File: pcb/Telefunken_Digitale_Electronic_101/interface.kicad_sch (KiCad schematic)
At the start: 7 parts, among them J10 Conn_01x03_Socket, J6 Conn_01x02_Socket, J7 Conn_01x02_Socket, J8 Conn_01x04_Socket, J9 Conn_01x04_Socket

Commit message: PCB: initial layout idea
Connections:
- net BT_FAST: now also J9.3 (Pin_3); no longer J10.3 (Pin_3)
- net BT_ILLUM: now also J9.2 (Pin_2); no longer J9.1 (Pin_1)
- net BT_SIGNAL: now also J10.3 (Pin_3); no longer J9.3 (Pin_3)
- net BT_SLEEP_FRONT: now also J9.1 (Pin_1); no longer J9.2 (Pin_2)
- net BT_SLOW: now also J9.4 (Pin_4); no longer J10.2 (Pin_2)
- net BT_TIME: now also J10.2 (Pin_2); no longer J9.4 (Pin_4)
- net RTC_SCL: now also J8.2 (Pin_2); no longer J8.1 (Pin_1)
- net RTC_SDA: now also J8.1 (Pin_1); no longer J8.2 (Pin_2)
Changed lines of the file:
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@@
-		)
-	)
-	(label "BT_SIGNAL"
-		(at 48.26 111.76 0)
-		(effects
-			(font
-				(size 1.27 1.27)
-			)
-			(justify left bottom)
 		)
 	)
 	(label "RTC_SDA"
-		(at 48.26 91.44 0)
+		(at 48.26 93.98 0)
 		(effects
 			(font
@@
 		)
 	)
+	(label "BT_ILLUM"
+		(at 48.26 114.3 0)
+		(effects
+			(font
+				(size 1.27 1.27)
+			)
+			(justify left bottom)
+		)
+	)
+	(label "BT_SIGNAL"
+		(at 48.26 128.27 0)
+		(effects
+			(font
+				(size 1.27 1.27)
+			)
+			(justify left bottom)
+		)
+	)
 	(label "BT_SLEEP_FRONT"
 		(at 107.95 114.3 0)
@@
 		)
 	)
+	(label "BT_SLOW"
+		(at 48.26 109.22 0)
+		(effects
+			(font
+				(size 1.27 1.27)
+			)
+			(justify left bottom)
+		)
+	)
 	(label "RTC_32K"
 		(at 106.68 85.09 0)
@@
 		)
 	)
-	(label "BT_TIME"
-		(at 48.26 109.22 0)
-		(effects
-			(font
-				(size 1.27 1.27)
-			)
-			(justify left bottom)
-		)
-	)
 	(label "BT_SLEEP_FRONT"
-		(at 48.26 114.3 0)
+		(at 48.26 116.84 0)
 		(effects
 			(font
@@
 		)
 	)
-	(label "BT_FAST"
-		(at 48.26 128.27 0)
-		(effects
-			(font
-				(size 1.27 1.27)
-			)
-			(justify left bottom)
-		)
-	)
 	(label "DISPLAY_CLK"
 		(at 102.87 68.58 0)
@@
 		)
 	)
+	(label "BT_TIME"
+		(at 48.26 130.81 0)
+		(effects
+			(font
+				(size 1.27 1.27)
+			)
+			(justify left bottom)
+		)
+	)
 	(label "RTC_SCL"
 		(at 106.68 92.71 0)
@@
 	)
 	(label "RTC_SCL"
-		(at 48.26 93.98 0)
+		(at 48.26 91.44 0)
 		(effects
 			(font
@@
 		)
 	)
+	(label "BT_FAST"
+		(at 48.26 111.76 0)
+		(effects
+			(font
+				(size 1.27 1.27)
+			)
+			(justify left bottom)
+		)
+	)
 	(label "BT_SLEEP_TOP"
 		(at 48.26 133.35 0)
@@
 		(effects
 			(font
-				(size 1.27 1.27)
-			)
-			(justify left bottom)
-		)
-	)
-	(label "BT_SLOW"
-		(at 48.26 130.81 0)
-		(effects
-			(font
-				(size 1.27 1.27)
-			)
-			(justify left bottom)
-		)
-	)
-	(label "BT_ILLUM"
-		(at 48.26 116.84 0)
-		(effects
-			(font

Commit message: SCH - buttons, display and interface: TM1637 can read the buttons (saves many resistors, caps and connectors)
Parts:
- removed J10: Conn_01x03_Socket, Connector_JST:JST_GH_BM03B-GHS-TBT_1x03-1MP_P1.25mm_Vertical, symbol Connector:Conn_01x03_Socket
- removed J9: Conn_01x04_Socket, Connector_JST:JST_GH_BM04B-GHS-TBT_1x04-1MP_P1.25mm_Vertical, symbol Connector:Conn_01x04_Socket

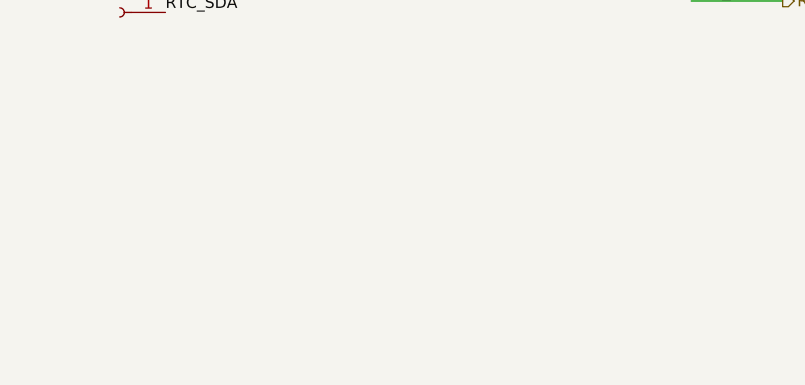
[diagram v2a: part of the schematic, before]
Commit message: SCH and PCB: added the Mounting Pads (a few chosen ones)
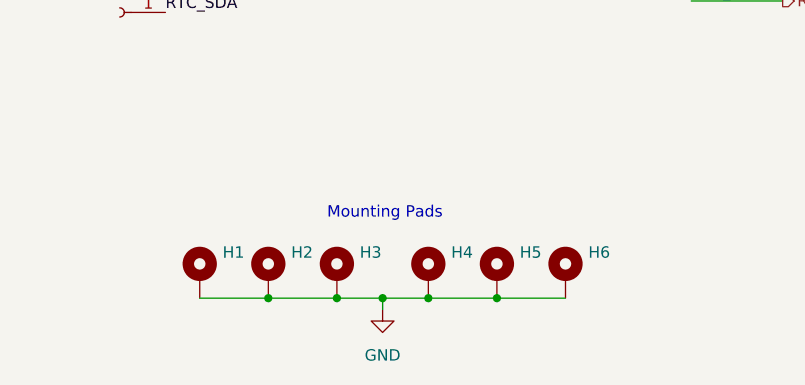
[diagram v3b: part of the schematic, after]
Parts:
- added H1, H2, H3, H4, H5, H6: MountingHole_Pad_MP, RadioWecker:BOARD_TO_BOARD_PAD_SMD, symbol Mechanical:MountingHole_Pad_MP
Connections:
- net GND: now also H1.MP, H2.MP, H3.MP, H4.MP, H5.MP, H6.MP
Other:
- note added: "Mounting Pads"

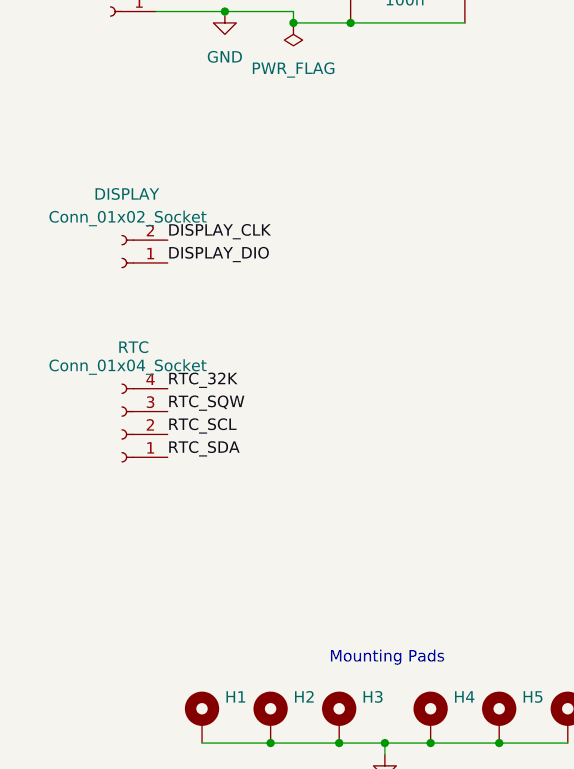
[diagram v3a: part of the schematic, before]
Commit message: SCH - interface: replaced symbols from connectors with mounting pads to contain the mounting pads (and connected them to GND)
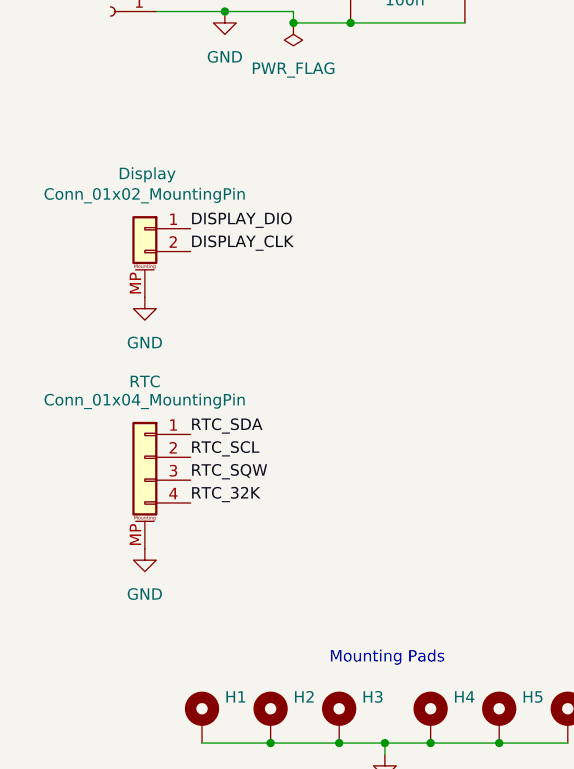
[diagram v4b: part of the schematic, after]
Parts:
- removed J7: Conn_01x02_Socket, Connector_JST:JST_GH_BM02B-GHS-TBT_1x02-1MP_P1.25mm_Vertical, symbol Connector:Conn_01x02_Socket
- removed J8: Conn_01x04_Socket, Connector_JST:JST_GH_BM04B-GHS-TBT_1x04-1MP_P1.25mm_Vertical, symbol Connector:Conn_01x04_Socket
- added J7: Conn_01x02_MountingPin, Connector_JST:JST_GH_BM02B-GHS-TBT_1x02-1MP_P1.25mm_Vertical, symbol Connector_Generic_MountingPin:Conn_01x02_MountingPin
- added J8: Conn_01x04_MountingPin, Connector_JST:JST_GH_BM04B-GHS-TBT_1x04-1MP_P1.25mm_Vertical, symbol Connector_Generic_MountingPin:Conn_01x04_MountingPin
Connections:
- net DISPLAY_CLK: now also J7.2 (Pin_2)
- net DISPLAY_DIO: now also J7.1 (Pin_1)
- net GND: now also J7.MP (MountPin), J8.MP (MountPin)
- net RTC_32K: now also J8.4 (Pin_4)
- net RTC_SCL: now also J8.2 (Pin_2)
- net RTC_SDA: now also J8.1 (Pin_1)
- net RTC_SQW: now also J8.3 (Pin_3)

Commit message: SCH and PCB: reannotated everything
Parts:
- renumbered C11 to C1, C12 to C2, J6 to J1, J7 to J2, J8 to J3
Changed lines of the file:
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@@
 		(in_pos_files yes)
 		(dnp no)
-		(property "Reference" "J8"
+		(property "Reference" "J3"
 			(at 45.72 85.09 0)
 			(hide yes)
@@
 			(project "Telefunken_Digitale_Electronic_101"
 				(path "/df1af5ff-c8b9-4769-9610-ead9e11e7e65/75a1a5d9-cb48-4e12-a237-e00fbc51bad9"
-					(reference "J8")
+					(reference "J3")
 					(unit 1)
 				)
@@
 		(dnp no)
 		(fields_autoplaced yes)
-		(property "Reference" "#PWR020"
+		(property "Reference" "#PWR03"
 			(at 54.61 45.72 0)
 			(hide yes)
@@
 			(project "Telefunken_Digitale_Electronic_101"
 				(path "/df1af5ff-c8b9-4769-9610-ead9e11e7e65/75a1a5d9-cb48-4e12-a237-e00fbc51bad9"
-					(reference "#PWR020")
+					(reference "#PWR03")
 					(unit 1)
 				)
@@
 		(dnp no)
 		(fields_autoplaced yes)
-		(property "Reference" "#PWR021"
+		(property "Reference" "#PWR04"
 			(at 54.61 50.8 0)
 			(hide yes)
@@
 			(project "Telefunken_Digitale_Electronic_101"
 				(path "/df1af5ff-c8b9-4769-9610-ead9e11e7e65/75a1a5d9-cb48-4e12-a237-e00fbc51bad9"
-					(reference "#PWR021")
+					(reference "#PWR04")
 					(unit 1)
 				)
@@
 		(in_pos_files yes)
 		(dnp no)
-		(property "Reference" "J7"
+		(property "Reference" "J2"
 			(at 45.72 62.23 0)
 			(hide yes)
@@
 			(project "Telefunken_Digitale_Electronic_101"
 				(path "/df1af5ff-c8b9-4769-9610-ead9e11e7e65/75a1a5d9-cb48-4e12-a237-e00fbc51bad9"
-					(reference "J7")
+					(reference "J2")
 					(unit 1)
 				)
@@
 		(dnp no)
 		(fields_autoplaced yes)
-		(property "Reference" "#PWR030"
+		(property "Reference" "#PWR02"
 			(at 45.72 110.49 0)
 			(hide yes)
@@
 			(project "Telefunken_Digitale_Electronic_101"
 				(path "/df1af5ff-c8b9-4769-9610-ead9e11e7e65/75a1a5d9-cb48-4e12-a237-e00fbc51bad9"
-					(reference "#PWR030")
+					(reference "#PWR02")
 					(unit 1)
 				)
@@
 		(dnp no)
 		(fields_autoplaced yes)
-		(property "Reference" "C11"
+		(property "Reference" "C1"
 			(at 72.39 40.6399 0)
 			(show_name no)
@@
 			(project "Telefunken_Digitale_Electronic_101"
 				(path "/df1af5ff-c8b9-4769-9610-ead9e11e7e65/75a1a5d9-cb48-4e12-a237-e00fbc51bad9"
-					(reference "C11")
+					(reference "C1")
 					(unit 1)
 				)
@@
 		(dnp no)
 		(fields_autoplaced yes)
-		(property "Reference" "#PWR025"
+		(property "Reference" "#PWR06"
 			(at 113.03 52.07 0)
 			(hide yes)
@@
 			(project "Telefunken_Digitale_Electronic_101"
 				(path "/df1af5ff-c8b9-4769-9610-ead9e11e7e65/75a1a5d9-cb48-4e12-a237-e00fbc51bad9"
-					(reference "#PWR025")
+					(reference "#PWR06")
 					(unit 1)
 				)
@@
 		(dnp no)
 		(fields_autoplaced yes)
-		(property "Reference" "#PWR022"
+		(property "Reference" "#PWR05"
 			(at 72.39 133.35 0)
 			(hide yes)
@@
 			(project "Telefunken_Digitale_Electronic_101"
 				(path "/df1af5ff-c8b9-4769-9610-ead9e11e7e65/75a1a5d9-cb48-4e12-a237-e00fbc51bad9"
-					(reference "#PWR022")
+					(reference "#PWR05")
 					(unit 1)
 				)
@@
 		(dnp no)
 		(fields_autoplaced yes)
-		(property "Reference" "C12"
+		(property "Reference" "C2"
 			(at 85.09 39.7509 0)
 			(show_name no)
@@
 			(project "Telefunken_Digitale_Electronic_101"
 				(path "/df1af5ff-c8b9-4769-9610-ead9e11e7e65/75a1a5d9-cb48-4e12-a237-e00fbc51bad9"
-					(reference "C12")
+					(reference "C2")
 					(unit 1)
 				)
@@
 		(dnp no)
 		(fields_autoplaced yes)
-		(property "Reference" "#PWR029"
+		(property "Reference" "#PWR01"
 			(at 45.72 82.55 0)
 			(hide yes)
@@
 			(project "Telefunken_Digitale_Electronic_101"
 				(path "/df1af5ff-c8b9-4769-9610-ead9e11e7e65/75a1a5d9-cb48-4e12-a237-e00fbc51bad9"
-					(reference "#PWR029")
+					(reference "#PWR01")
 					(unit 1)
 				)
@@
 		(in_pos_files yes)
 		(dnp no)
-		(property "Reference" "J6"
+		(property "Reference" "J1"
 			(at 42.545 36.83 0)
 			(hide yes)
@@
 			(project "Telefunken_Digitale_Electronic_101"
 				(path "/df1af5ff-c8b9-4769-9610-ead9e11e7e65/75a1a5d9-cb48-4e12-a237-e00fbc51bad9"
-					(reference "J6")
+					(reference "J1")
 					(unit 1)
 				)
@@
 		(dnp no)
 		(fields_autoplaced yes)
-		(property "Reference" "#PWR026"
+		(property "Reference" "#PWR07"
 			(at 113.03 58.42 0)
 			(hide yes)
@@
 			(project "Telefunken_Digitale_Electronic_101"
 				(path "/df1af5ff-c8b9-4769-9610-ead9e11e7e65/75a1a5d9-cb48-4e12-a237-e00fbc51bad9"
-					(reference "#PWR026")
-					(unit 1)
-				)
+					(reference "#PWR07")
+					(unit 1)
+				)

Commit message: adjusted connectors footprints, added footprint to input polarized capacitor, rtc and display polarized capacitors converted to non polarized
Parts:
- removed J1: Conn_01x02_Socket, Connector_JST:JST_XH_B2B-XH-A_1x02_P2.50mm_Vertical, symbol Connector:Conn_01x02_Socket
- added J1: Conn_01x02_MountingPin, RadioWecker:JST_S2B-XH-SM4-TB, symbol Connector_Generic_MountingPin:Conn_01x02_MountingPin
- C2: footprint (none) -> Capacitor_THT:CP_Radial_D4.0mm_P2.00mm
- J2: footprint Connector_JST:JST_GH_BM02B-GHS-TBT_1x02-1MP_P1.25mm_Vertical -> Connector_Molex:Molex_PicoBlade_53261-0271_1x02-1MP_P1.25mm_Horizontal
- J3: footprint Connector_JST:JST_GH_BM04B-GHS-TBT_1x04-1MP_P1.25mm_Vertical -> Connector_Molex:Molex_PicoBlade_53261-0471_1x04-1MP_P1.25mm_Horizontal
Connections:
- net GND: now also J1.2 (Pin_2), J1.MP (MountPin)
- net VCC: now also J1.1 (Pin_1)
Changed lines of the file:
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@@
 			)
 		)
-		(property "Footprint" "Connector_JST:JST_GH_BM04B-GHS-TBT_1x04-1MP_P1.25mm_Vertical"
+		(property "Footprint" "Connector_Molex:Molex_PicoBlade_53261-0471_1x04-1MP_P1.25mm_Horizontal"
 			(at 45.72 93.98 0)
 			(hide yes)
@@
 			)
 		)
-		(property "Footprint" "Connector_JST:JST_GH_BM02B-GHS-TBT_1x02-1MP_P1.25mm_Vertical"
+		(property "Footprint" "Connector_Molex:Molex_PicoBlade_53261-0271_1x02-1MP_P1.25mm_Horizontal"
 			(at 45.72 68.58 0)
 			(hide yes)
@@
 	)
 	(symbol
+		(lib_id "Connector_Generic_MountingPin:Conn_01x02_MountingPin")
+		(at 41.91 41.91 0)
+		(mirror y)
+		(unit 1)
+		(body_style 1)
+		(exclude_from_sim no)
+		(in_bom yes)
+		(on_board yes)
+		(in_pos_files yes)
+		(dnp no)
+		(property "Reference" "J1"
+			(at 41.91 35.56 0)
+			(hide yes)
+			(show_name no)
+			(do_not_autoplace no)
+			(effects
+				(font
+					(size 1.27 1.27)
+				)
+			)
+		)
+		(property "Value" "Conn_01x02_MountingPin"
+			(at 41.91 38.1 0)
+			(show_name no)
+			(do_not_autoplace no)
+			(effects
+				(font
+					(size 1.27 1.27)
+				)
+			)
+		)
+		(property "Footprint" "RadioWecker:JST_S2B-XH-SM4-TB"
+			(at 41.91 41.91 0)
+			(hide yes)
+			(show_name no)
+			(do_not_autoplace no)
+			(effects
+				(font
+					(size 1.27 1.27)
+				)
+			)
+		)
+		(property "Datasheet" ""
+			(at 41.91 41.91 0)
+			(hide yes)
+			(show_name no)
+			(do_not_autoplace no)
+			(effects
+				(font
+					(size 1.27 1.27)
+				)
+			)
+		)
+		(property "Description" "Generic connectable mounting pin connector, single row, 01x02, script generated (kicad-library-utils/schlib/autogen/connector/)"
+			(at 41.91 41.91 0)
+			(hide yes)
+			(show_name no)
+			(do_not_autoplace no)
+			(effects
+				(font
+					(size 1.27 1.27)
+				)
+			)
+		)
+		(property "Name" "POWER"
+			(at 42.164 35.814 0)
+			(show_name no)
+			(do_not_autoplace no)
+			(effects
+				(font
+					(size 1.27 1.27)
+				)
+			)
+		)
+		(pin "1"
+		)
+		(pin "2"
+		)
+		(pin "MP"
+		)
+		(instances
+			(project "Telefunken_Digitale_Electronic_101"
+				(path "/df1af5ff-c8b9-4769-9610-ead9e11e7e65/75a1a5d9-cb48-4e12-a237-e00fbc51bad9"
+					(reference "J1")
+					(unit 1)
+				)
+			)
+		)
+	)
+	(symbol
 		(lib_id "Mechanical:MountingHole_Pad_MP")
 		(at 77.47 123.19 0)
@@
 	(symbol
 		(lib_id "power:GND")
+		(at 41.91 49.53 0)
+		(unit 1)
+		(body_style 1)
+		(exclude_from_sim no)
+		(in_bom yes)
+		(on_board yes)
+		(in_pos_files yes)
+		(dnp no)
+		(fields_autoplaced yes)
+		(property "Reference" "#PWR023"
+			(at 41.91 55.88 0)
+			(hide yes)
+			(show_name no)
+			(do_not_autoplace no)
+			(effects
+				(font
+					(size 1.27 1.27)
+				)
+			)
+		)
+		(property "Value" "GND"
+			(at 41.91 54.61 0)
+			(show_name no)
+			(do_not_autoplace no)
+			(effects
+				(font
+					(size 1.27 1.27)
+				)
+			)
+		)
+		(property "Footprint" ""
+			(at 41.91 49.53 0)
+			(hide yes)
+			(show_name no)
+			(do_not_autoplace no)
+			(effects
+				(font
+					(size 1.27 1.27)
+				)
+			)
+		)
+		(property "Datasheet" ""
+			(at 41.91 49.53 0)
+			(hide yes)
+			(show_name no)
+			(do_not_autoplace no)
+			(effects
+				(font
+					(size 1.27 1.27)
+				)
+			)
+		)
+		(property "Description" "Power symbol creates a global label with name \"GND\" , ground"
+			(at 41.91 49.53 0)
+			(hide yes)
+			(show_name no)
+			(do_not_autoplace no)
+			(effects
+				(font
+					(size 1.27 1.27)
+				)
+			)
+		)
+		(pin "1"
+		)
+		(instances
+			(project "Telefunken_Digitale_Electronic_101"
+				(path "/df1af5ff-c8b9-4769-9610-ead9e11e7e65/75a1a5d9-cb48-4e12-a237-e00fbc51bad9"
+					(reference "#PWR023")
+					(unit 1)
+				)
+			)
+		)
+	)
+	(symbol
+		(lib_id "power:GND")
 		(at 45.72 104.14 0)
 		(unit 1)
@@
 			)
 		)
-		(property "Footprint" ""
+		(property "Footprint" "Capacitor_THT:CP_Radial_D4.0mm_P2.00mm"
 			(at 82.2452 45.72 0)
 			(hide yes)
@@
 					(unit 1)
 				)
-			)
-		)
-	)
-	(symbol
-		(lib_id "Connector:Conn_01x02_Socket")
-		(at 41.91 44.45 180)
-		(unit 1)
-		(body_style 1)
-		(exclude_from_sim no)
-		(in_bom yes)
-		(on_board yes)
-		(in_pos_files yes)
-		(dnp no)
-		(property "Reference" "J1"
-			(at 42.545 36.83 0)
-			(hide yes)
-			(show_name no)
-			(do_not_autoplace no)
-			(effects
-				(font
-					(size 1.27 1.27)
-				)
-			)
-		)
-		(property "Value" "Conn_01x02_Socket"
-			(at 42.545 39.37 0)
-			(show_name no)
-			(do_not_autoplace no)
-			(effects
-				(font
-					(size 1.27 1.27)
-				)
-			)
-		)
-		(property "Footprint" "Connector_JST:JST_XH_B2B-XH-A_1x02_P2.50mm_Vertical"
-			(at 41.91 44.45 0)
-			(hide yes)
-			(show_name no)
-			(do_not_autoplace no)
-			(effects
-				(font
-					(size 1.27 1.27)
-				)
-			)
-		)
-		(property "Datasheet" ""
-			(at 41.91 44.45 0)
-			(hide yes)
-			(show_name no)
-			(do_not_autoplace no)
-			(effects
-				(font
-					(size 1.27 1.27)
-				)
-			)
-		)
-		(property "Description" "Generic connector, single row, 01x02, script generated"
-			(at 41.91 44.45 0)
-			(hide yes)
-			(show_name no)
-			(do_not_autoplace no)
-			(effects
-				(font
-					(size 1.27 1.27)
-				)
-			)
-		)
-		(property "Name" "POWER"
-			(at 42.672 37.084 0)
-			(show_name no)
-			(do_not_autoplace no)
-			(effects
-				(font
-					(size 1.27 1.27)
-				)
-			)
-		)
-		(pin "1"
-		)
-		(pin "2"
-		)
-		(instances
-			(project "Telefunken_Digitale_Electronic_101"
-				(path "/df1af5ff-c8b9-4769-9610-ead9e11e7e65/75a1a5d9-cb48-4e12-a237-e00fbc51bad9"
-					(reference "J1")
-					(unit 1)
-				)
